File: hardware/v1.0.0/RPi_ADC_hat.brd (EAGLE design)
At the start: 65 x 56 mm, 61 parts, among them Q1 FDT439N, Q2 FDT439N, U1 MCP1790, U2 NME0509SC, U3 HIH6131, U4 MCP3424, U5 PCA9517A, U6 LM61 *, U7 C24C32, X1 I2C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

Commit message: Increase gate resistors, renumber parts
Resistors on FET gate increased to more closely match the value
that would be needed if the FET is replaced by a BJT.
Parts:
- JP1: value I2C ADDRESS -> I2C VIN; device pinhead:2X03 -> SparkFun:1X03
- JP2: value PROG -> I2C ADDRESS; device SparkFun:1X02 -> pinhead:2X03
- JP3: value I2C VIN -> PROG; device SparkFun:1X03 -> SparkFun:1X02
- R10, R11: value 330R -> 560R
- moved JP3 43.3 mm to (35.6, 40.6)
- moved JP1 23.9 mm to (7.62, 7.62), turned to 270 degrees
- moved JP2 21.1 mm to (17.8, 29.2), turned to 90 degrees
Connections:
- net 5V_PI: now also JP1.1; no longer JP3.1
- net AVCC: now also JP2.1, JP2.2; no longer JP1.1, JP1.2
- net DC-DC_OUT: now also JP1.3; no longer JP3.3
- net EEPROM_WP: now also JP3.1; no longer JP2.1
- net GND: now also JP2.5, JP2.6, JP3.2; no longer JP1.5, JP1.6, JP2.2
- net I2C_VIN: now also JP1.2; no longer JP3.2
- net N$16: now also JP2.4; no longer JP1.4
- net N$6: now also JP2.3; no longer JP1.3
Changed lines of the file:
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@@
 <attribute name="VALUE" x="41.275" y="27.94" size="1.016" layer="27" ratio="10"/>
 </element>
-<element name="R10" library="SteveMarple" package="1206-HAND" value="330R" x="38.1" y="33.02" smashed="yes" rot="R90">
+<element name="R10" library="SteveMarple" package="1206-HAND" value="560R" x="38.1" y="33.02" smashed="yes" rot="R90">
 <attribute name="NAME" x="36.83" y="29.21" size="1.016" layer="25" ratio="10"/>
 <attribute name="VALUE" x="36.83" y="27.94" size="1.016" layer="27" ratio="10"/>
@@
 <attribute name="VALUE" x="41.275" y="40.64" size="1.016" layer="27" ratio="10"/>
 </element>
-<element name="R11" library="SteveMarple" package="1206-HAND" value="330R" x="37.465" y="46.99" smashed="yes">
+<element name="R11" library="SteveMarple" package="1206-HAND" value="560R" x="37.465" y="46.99" smashed="yes">
 <attribute name="NAME" x="36.83" y="44.45" size="1.016" layer="25" ratio="10"/>
 <attribute name="VALUE" x="36.83" y="43.18" size="1.016" layer="27" ratio="10"/>
@@
 <attribute name="VALUE" x="17.78" y="14.605" size="1.016" layer="28" ratio="10" rot="MR0"/>
 </element>
-<element name="JP1" library="pinhead" package="2X03" value="I2C ADDRESS" x="17.78" y="29.21" smashed="yes" rot="R90">
+<element name="JP2" library="pinhead" package="2X03" value="I2C ADDRESS" x="17.78" y="29.21" smashed="yes" rot="R90">
 <attribute name="NAME" x="26.035" y="32.639" size="1.27" layer="25" ratio="10"/>
 </element>
@@
 <attribute name="VALUE" x="50.165" y="25.4" size="1.016" layer="28" ratio="10" rot="MR0"/>
 </element>
-<element name="JP2" library="SparkFun" package="1X02" value="PROG" x="35.56" y="40.64" smashed="yes" rot="R270">
+<element name="JP3" library="SparkFun" package="1X02" value="PROG" x="35.56" y="40.64" smashed="yes" rot="R270">
 <attribute name="NAME" x="38.735" y="36.83" size="1.27" layer="25" ratio="10" rot="R90"/>
 <attribute name="VALUE" x="40.64" y="36.83" size="1.27" layer="27" ratio="10" rot="R90"/>
@@
 <attribute name="NAME" x="16.51" y="33.02" size="1.016" layer="26" ratio="10" rot="MR0"/>
 </element>
-<element name="JP3" library="SparkFun" package="1X03" value="I2C VIN" x="7.62" y="7.62" smashed="yes" rot="R270">
+<element name="JP1" library="SparkFun" package="1X03" value="I2C VIN" x="7.62" y="7.62" smashed="yes" rot="R270">
 <attribute name="NAME" x="3.175" y="8.255" size="1.016" layer="25" ratio="10"/>
 <attribute name="VALUE" x="0" y="6.985" size="1.016" layer="27" ratio="10"/>
@@
 <contactref element="C12" pad="2"/>
 <contactref element="C11" pad="2"/>
-<contactref element="JP1" pad="6"/>
-<contactref element="JP1" pad="5"/>
+<contactref element="JP2" pad="6"/>
+<contactref element="JP2" pad="5"/>
 <contactref element="U1" pad="2"/>
 <contactref element="U1" pad="2"/>
@@
 <wire x1="25.4" y1="32.385" x2="25.4" y2="26.67" width="0.381" layer="1"/>
 <wire x1="22.225" y1="35.56" x2="25.4" y2="32.385" width="0.381" layer="1"/>
-<contactref element="JP2" pad="2"/>
+<contactref element="JP3" pad="2"/>
 <wire x1="40.005" y1="40.869" x2="40.005" y2="42.545" width="0.381" layer="16"/>
 <wire x1="40.005" y1="42.545" x2="42.545" y2="42.545" width="0.381" layer="16"/>
@@
 <wire x1="5.08" y1="33.02" x2="5.08" y2="31.75" width="0.381" layer="1"/>
 <wire x1="5.842" y1="29.21" x2="5.944" y2="29.21" width="0.381" layer="1"/>
-<contactref element="JP3" pad="1"/>
+<contactref element="JP1" pad="1"/>
 <contactref element="U$7" pad="1"/>
 <wire x1="57.15" y1="8.89" x2="59.69" y2="8.89" width="0.381" layer="1"/>
@@
 <contactref element="U4" pad="6"/>
 <contactref element="C6" pad="1"/>
-<contactref element="JP1" pad="2"/>
-<contactref element="JP1" pad="1"/>
+<contactref element="JP2" pad="2"/>
+<contactref element="JP2" pad="1"/>
 <contactref element="U1" pad="3"/>
 <wire x1="33.02" y1="29.439" x2="33.02" y2="29.21" width="0.381" layer="1"/>
@@
 <signal name="N$6">
 <contactref element="U4" pad="9"/>
-<contactref element="JP1" pad="3"/>
+<contactref element="JP2" pad="3"/>
 <wire x1="20.32" y1="27.94" x2="22.7838" y2="27.94" width="0.254" layer="1"/>
 <wire x1="19.05" y1="29.21" x2="20.32" y2="27.94" width="0.254" layer="1"/>
 </signal>
 <signal name="N$16">
-<contactref element="JP1" pad="4"/>
+<contactref element="JP2" pad="4"/>
 <contactref element="U4" pad="10"/>
 <wire x1="21.59" y1="26.67" x2="22.7838" y2="26.67" width="0.254" layer="1"/>
@@
 <wire x1="12.7" y1="17.78" x2="12.7" y2="22.86" width="0.381" layer="1"/>
 <wire x1="12.7" y1="22.86" x2="12.294" y2="22.86" width="0.381" layer="1"/>
-<contactref element="JP3" pad="3"/>
+<contactref element="JP1" pad="3"/>
 <wire x1="7.62" y1="2.54" x2="5.969" y2="4.191" width="0.381" layer="16"/>
 <wire x1="5.969" y1="4.191" x2="5.969" y2="9.779" width="0.381" layer="16"/>
@@
 <contactref element="R7" pad="1"/>
 <contactref element="U7" pad="7"/>
-<contactref element="JP2" pad="1"/>
+<contactref element="JP3" pad="1"/>
 <wire x1="41.91" y1="31.979" x2="41.91" y2="33.02" width="0.254" layer="16"/>
 <wire x1="41.91" y1="33.02" x2="43.815" y2="34.925" width="0.254" layer="16"/>
@@
 </signal>
 <signal name="I2C_VIN" class="1">
-<contactref element="JP3" pad="2"/>
+<contactref element="JP1" pad="2"/>
 <contactref element="X1" pad="1"/>
 <wire x1="7.62" y1="5.08" x2="8.89" y2="5.08" width="0.381" layer="16"/>

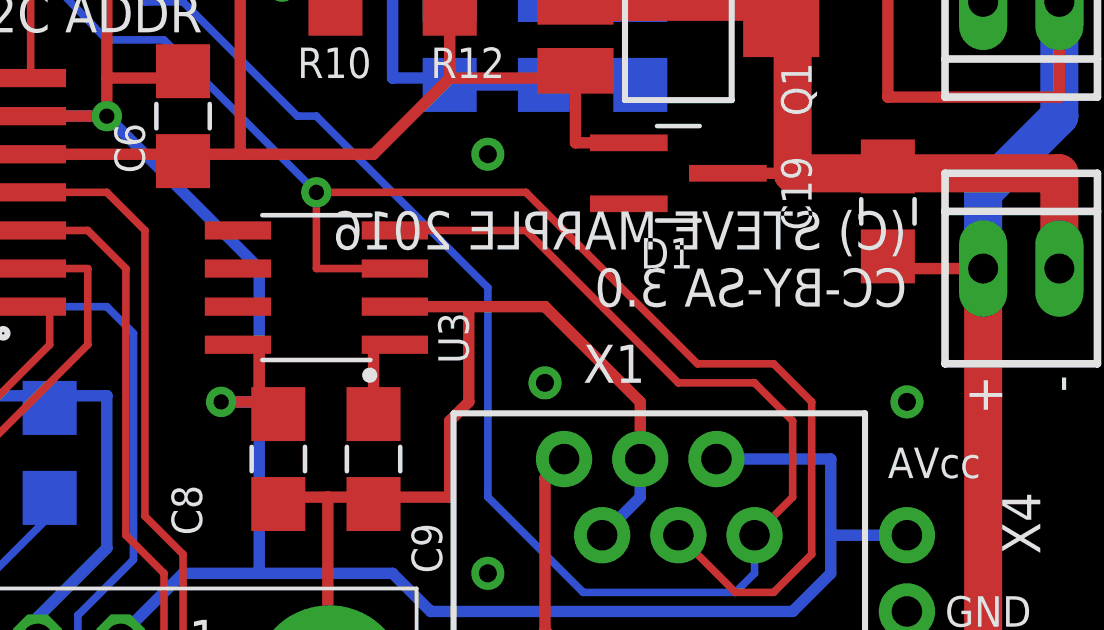
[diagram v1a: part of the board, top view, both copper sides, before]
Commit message: Minor fixes to silkscreen
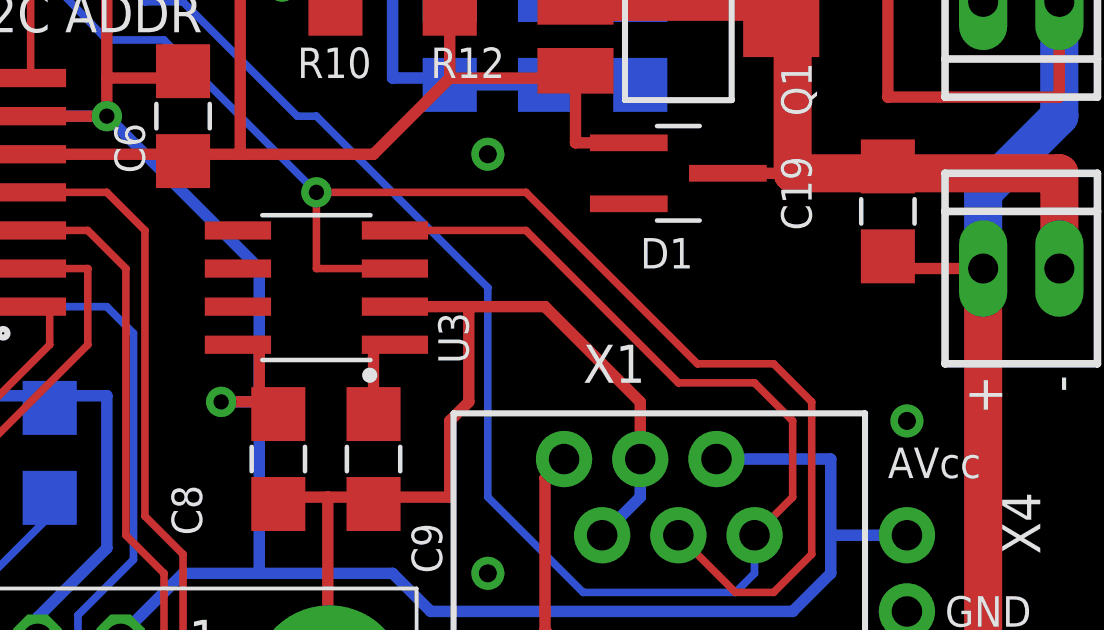
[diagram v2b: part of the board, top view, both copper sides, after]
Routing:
- net GND: vias 19 -> 18
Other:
- board text added: "(C) Steve Marple 2016"
- board text added: "Raspberry Pi ADC hat"
- board text removed: "(C) STEVE MARPLE 2016"
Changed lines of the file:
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@@
 <text x="62.23" y="35.306" size="1.27" layer="121" ratio="10" rot="R90" align="center-left">+</text>
 <text x="59.69" y="35.306" size="1.27" layer="121" ratio="10" rot="R90" align="center-left">-</text>
-<text x="57.15" y="21.59" size="1.27" layer="121" ratio="10" rot="MR0">CC-BY-SA 3.0</text>
-<text x="57.15" y="23.495" size="1.27" layer="121" ratio="10" rot="MR0">(C) STEVE MARPLE 2016</text>
-<text x="57.15" y="19.685" size="1.016" layer="122" ratio="10" rot="MR0">https://github.com/stevemarple/RPi_ADC_hat</text>
+<text x="57.15" y="19.05" size="1.27" layer="122" ratio="10" rot="MR0">CC-BY-SA 3.0</text>
+<text x="57.15" y="20.955" size="1.27" layer="122" ratio="10" rot="MR0">(C) Steve Marple 2016</text>
+<text x="0" y="7.62" size="1.016" layer="122" ratio="10" rot="MR90">https://github.com/stevemarple/RPi_ADC_hat</text>
 <text x="56.515" y="15.875" size="1.016" layer="121" ratio="10">AVcc</text>
 <text x="58.42" y="11.43" size="1.016" layer="121" ratio="10" align="center-left">GND</text>
 <text x="58.42" y="6.985" size="1.016" layer="121" ratio="10">5V
 (RPi)</text>
+<text x="57.15" y="22.86" size="1.27" layer="122" ratio="10" rot="MR0">Raspberry Pi ADC hat</text>
 </plain>
 <attributes>
@@
 <via x="43.18" y="26.67" extent="1-16" drill="0.6"/>
 <via x="48.895" y="8.89" extent="1-16" drill="0.6"/>
-<via x="45.085" y="19.05" extent="1-16" drill="0.6"/>
-<via x="57.15" y="18.415" extent="1-16" drill="0.6"/>
+<via x="57.15" y="17.78" extent="1-16" drill="0.6"/>
 <via x="60.325" y="41.275" extent="1-16" drill="0.6"/>
 <via x="57.15" y="46.99" extent="1-16" drill="0.6"/>
